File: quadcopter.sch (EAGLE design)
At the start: 11 parts, among them J1 AVR_SPI_PRG_6NS, U1 ATMEGA128RFA1

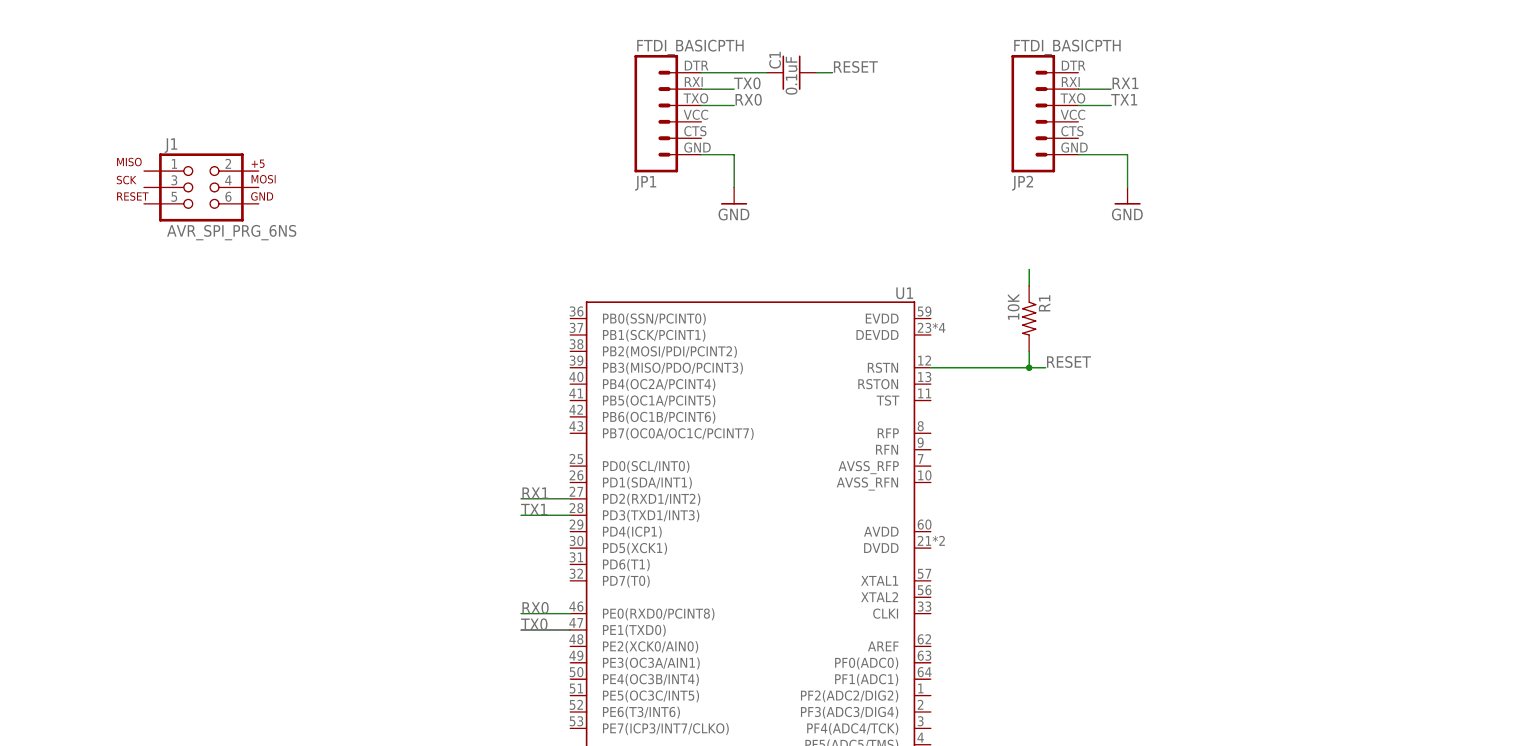
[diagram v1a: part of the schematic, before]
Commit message: finished, for the most part, microcontroller section
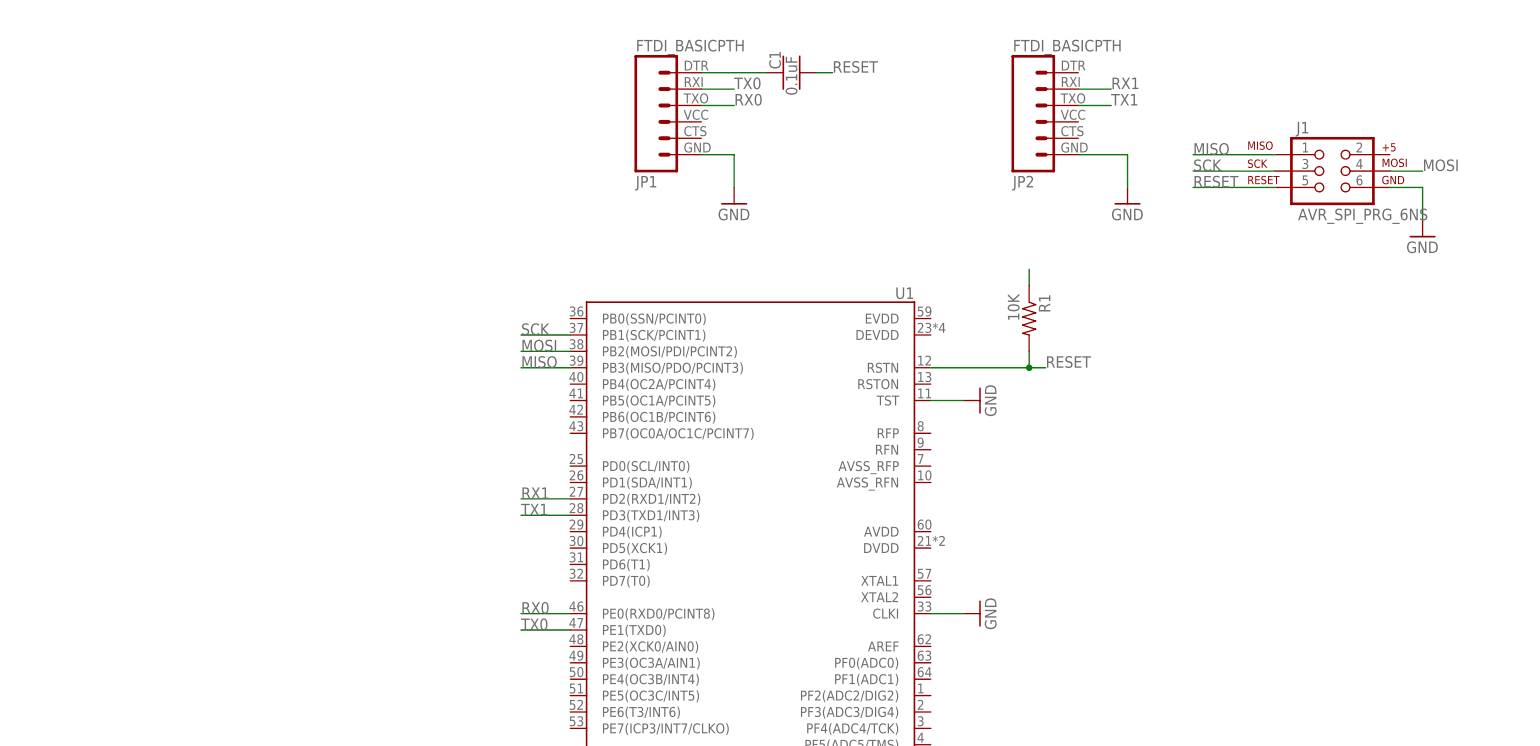
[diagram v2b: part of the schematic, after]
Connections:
- new net MISO: U1.PB3(MISO/PDO/PCINT3)
- new net MOSI: U1.PB2(MOSI/PDI/PCINT2)
- new net N$11: J1.3
- new net N$12: J1.5
- new net N$8: J1.1
- new net N$9: J1.4
- new net SCK: U1.PB1(SCK/PCINT1)
- net GND: now also J1.6, U1.CLKI, U1.TST
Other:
- moved on the sheet: J1
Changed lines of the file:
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@@
 <part name="R1" library="quadparts_prebuilt" deviceset="RESISTOR_" device="SMD-2012-0805-10K" value="10K"/>
 <part name="GND2" library="quadparts_prebuilt" deviceset="GND" device=""/>
+<part name="GND3" library="quadparts_prebuilt" deviceset="GND" device=""/>
+<part name="GND4" library="quadparts_prebuilt" deviceset="GND" device=""/>
+<part name="GND5" library="quadparts_prebuilt" deviceset="GND" device=""/>
 </parts>
 <sheets>
@@
 <instance part="JP1" gate="G$1" x="-71.12" y="12.7" rot="MR180"/>
 <instance part="JP2" gate="G$1" x="-12.7" y="12.7" rot="MR180"/>
-<instance part="J1" gate="G$1" x="-144.78" y="0"/>
+<instance part="J1" gate="G$1" x="30.48" y="2.54"/>
 <instance part="U$1" gate="G$1" x="-20.32" y="60.96"/>
 <instance part="GND1" gate="1" x="-60.96" y="-2.54"/>
@@
 <instance part="R1" gate="G$1" x="-15.24" y="-20.32" rot="R270"/>
 <instance part="GND2" gate="1" x="0" y="-2.54"/>
+<instance part="GND3" gate="1" x="45.72" y="-7.62"/>
+<instance part="GND4" gate="1" x="-22.86" y="-33.02" rot="R90"/>
+<instance part="GND5" gate="1" x="-22.86" y="-66.04" rot="R90"/>
 </instances>
 <busses>
@@
 <wire x1="-7.62" y1="5.08" x2="0" y2="5.08" width="0.1524" layer="91"/>
 <wire x1="0" y1="5.08" x2="0" y2="0" width="0.1524" layer="91"/>
+</segment>
+<segment>
+<pinref part="J1" gate="G$1" pin="6"/>
+<pinref part="GND3" gate="1" pin="GND"/>
+<wire x1="40.64" y1="0" x2="45.72" y2="0" width="0.1524" layer="91"/>
+<wire x1="45.72" y1="0" x2="45.72" y2="-5.08" width="0.1524" layer="91"/>
+</segment>
+<segment>
+<pinref part="U1" gate="G$1" pin="TST"/>
+<pinref part="GND4" gate="1" pin="GND"/>
+<wire x1="-30.48" y1="-33.02" x2="-25.4" y2="-33.02" width="0.1524" layer="91"/>
+</segment>
+<segment>
+<pinref part="U1" gate="G$1" pin="CLKI"/>
+<pinref part="GND5" gate="1" pin="GND"/>
+<wire x1="-30.48" y1="-66.04" x2="-25.4" y2="-66.04" width="0.1524" layer="91"/>
 </segment>
 </net>
@@
 <pinref part="R1" gate="G$1" pin="2"/>
 <wire x1="-15.24" y1="-25.4" x2="-15.24" y2="-27.94" width="0.1524" layer="91"/>
+<label x="10.16" y="0" size="1.778" layer="95"/>
 </segment>
 </net>
@@
 </segment>
 </net>
+<net name="MOSI" class="0">
+<segment>
+<pinref part="U1" gate="G$1" pin="PB2(MOSI/PDI/PCINT2)"/>
+<wire x1="-86.36" y1="-25.4" x2="-93.98" y2="-25.4" width="0.1524" layer="91"/>
+<label x="45.72" y="2.54" size="1.778" layer="95"/>
+<label x="-93.98" y="-25.4" size="1.778" layer="95"/>
+</segment>
+</net>
+<net name="N$9" class="0">
+<segment>
+<pinref part="J1" gate="G$1" pin="4"/>
+<wire x1="40.64" y1="2.54" x2="45.72" y2="2.54" width="0.1524" layer="91"/>
+</segment>
+</net>
+<net name="N$8" class="0">
+<segment>
+<pinref part="J1" gate="G$1" pin="1"/>
+<wire x1="22.86" y1="5.08" x2="10.16" y2="5.08" width="0.1524" layer="91"/>
+</segment>
+</net>
+<net name="MISO" class="0">
+<segment>
+<pinref part="U1" gate="G$1" pin="PB3(MISO/PDO/PCINT3)"/>
+<wire x1="-86.36" y1="-27.94" x2="-93.98" y2="-27.94" width="0.1524" layer="91"/>
+<label x="10.16" y="5.08" size="1.778" layer="95"/>
+<label x="-93.98" y="-27.94" size="1.778" layer="95"/>
+</segment>
+</net>
+<net name="SCK" class="0">
+<segment>
+<pinref part="U1" gate="G$1" pin="PB1(SCK/PCINT1)"/>
+<wire x1="-86.36" y1="-22.86" x2="-93.98" y2="-22.86" width="0.1524" layer="91"/>
+<label x="10.16" y="2.54" size="1.778" layer="95"/>
+<label x="-93.98" y="-22.86" size="1.778" layer="95"/>
+</segment>
+</net>
+<net name="N$11" class="0">
+<segment>
+<pinref part="J1" gate="G$1" pin="3"/>
+<wire x1="22.86" y1="2.54" x2="10.16" y2="2.54" width="0.1524" layer="91"/>
+</segment>
+</net>
+<net name="N$12" class="0">
+<segment>
+<pinref part="J1" gate="G$1" pin="5"/>
+<wire x1="22.86" y1="0" x2="10.16" y2="0" width="0.1524" layer="91"/>
+</segment>
+</net>

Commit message: Sort of finished motor driver sch
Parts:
- added BATT1: BATTERY-HUBSAN-W/HOLDER, quadparts_prebuilt:BATTERY-HUBSAN-W/HOLDER
- added C2, C4, C6, C8: 100uF, quadparts_prebuilt:CAPACITOR-POL_SMD-7043-D_TANTALUM-220UF
- added C3, C5, C7, C9: 1uF, quadparts_prebuilt:CAPACITOR-NP_SMD-2012-0805_CERAMIC-1UF
- added D1, D2, D3, D4: 20V-500MA, quadparts_prebuilt:DIODE-SCHOTTKY_SMD-SOD123
- added J2: (no value), quadparts_connie:MALE_HEADER_2POS-2X1-0.1IN
- added Q1, Q2, Q3, Q4: (no value), quadparts_connie:N_MOSFET_SI2302CDS_T1_E3
- added R2, R4, R6, R8: 100R, quadparts_prebuilt:RESISTOR_SMD-2012-0805-100
- added R3, R5, R7, R9: 10K 1/10W, quadparts_prebuilt:RESISTOR_SMD-2012-0805-100
- added U$6: MOTOR_PADS, quadparts_prebuilt:MOTOR_PADS
- U$3: value MOTOR_PADS -> TPS73633-DBVT; device quadparts_prebuilt:MOTOR_PADS -> quadparts_prebuilt:TPS73633-DBVT
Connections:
- new net FILTERED: Q1.G, Q2.G, Q3.G, Q4.G, R2.2, R3.2, R4.2, R5.2, R6.2, R7.2, R8.2, R9.2
- new net FLYBACK: D1.A, D2.A, D3.A, D4.A, Q1.D, Q2.D, Q3.D, Q4.D, U$2.V-, U$4.V-, U$5.V-, U$6.V-
- new net N$10: C2.+, D1.C, U$2.V+
- new net N$13: C4.+, D2.C, U$4.V+
- new net N$14: C6.+, D3.C, U$5.V+
- new net N$15: C8.+, D4.C, U$6.V+
- new net N$16: U1.PB5(OC1A/PCINT5)
- new net PB5: C3.1, C5.1, C7.1, C9.1, R2.1, R4.1, R6.1, R8.1
- new net PE3: U1.PE3(OC3A/AIN1)
- new net PE4: U1.PE4(OC3B/INT4)
- new net PE5: U1.PE5(OC3C/INT5)
- net GND: now also C2.-, C3.2, C4.-, C5.2, C6.-, C7.2, C8.-, C9.2, Q1.S, Q2.S, Q3.S, Q4.S, R3.1, R5.1, R7.1, R9.1
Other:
- note added: "Filter"
- note added: "Flyback"
- moved on the sheet: R1, U$2, U$4, U$5, U1

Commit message: added stuff
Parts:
- added B1: BALUN0805, quadparts_prebuilt:BALUN0805
- added C10, C11, C12, C13: 1uF, quadparts_prebuilt:CAPACITOR-NP_SMD-2012-0805_CERAMIC-1UF
- added C14, C15: 12pF, quadparts_prebuilt:CAPACITOR-NP_SMD-2012-0805_CERAMIC-1UF
- added C16, C17: JUMP, quadparts_prebuilt:CAPACITOR-NP_SMD-2012-0805_CERAMIC
- added C18: 22pF, quadparts_prebuilt:CAPACITOR-NP_SMD-2012-0805_CERAMIC-22PF
- added C19: 0.75pF, quadparts_prebuilt:CAPACITOR-NP_SMD-2012-0805_CERAMIC-0.75PF
- added U$7: NET_BRIDGE, quadparts_jason:NET_BRIDGE
- added Y1: 16MHz, quadparts_prebuilt:CRYSTAL5X3
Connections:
- removed net N$15: C8.+, D4.C, U$6.V+
- new net 3V: C11.1, R1.1, U$3.OUT, U1.DEVDD, U1.EVDD
- new net BAT_GND: BATT1.N, C2.-, C3.2, C4.-, C5.2, C6.-, C7.2, C8.-, C9.2, Q1.S, Q2.S, Q3.S, Q4.S, R3.1, R5.1, R7.1, R9.1, U$7.P$2
- new net EN: J2.1, U$3.EN
- new net N$21: C16.1, U1.RFP
- new net N$22: C17.1, U1.RFN
- new net N$23: B1.IN, C16.2
- new net N$24: B1.GND@5, C17.2
- new net N$25: C18.1
- new net RFANT: B1.OUT1, C19.2, U$1.SIGNAL
- new net VBAT: BATT1.P, C10.1, C2.+, C4.+, C6.+, C8.+, D1.C, D2.C, D3.C, D4.C, U$2.V+, U$3.IN, U$4.V+, U$5.V+, U$6.V+
- net GND: now also B1.OUT2, C10.2, C11.2, C12.2, C13.2, C14.2, C15.2, C18.2, C19.1, J2.2, U$3.GND, U$3.NC/FB, U$7.P$1, U1.AVSS, U1.AVSS_RFN, U1.AVSS_RFP, U1.DVSS, U1.PG3(TOSC2), U1.PG4(TOSC1); no longer C2.-, C3.2, C4.-, C5.2, C6.-, C7.2, C8.-, C9.2, Q1.S, Q2.S, Q3.S, Q4.S, R3.1, R5.1, R7.1, R9.1
- net N$10: now also C12.1, U1.AVDD; no longer C2.+, D1.C, U$2.V+
- net N$13: now also C13.1, U1.DVDD; no longer C4.+, D2.C, U$4.V+
- net N$14: now also C14.1, U1.XTAL2, Y1.1; no longer C6.+, D3.C, U$5.V+
- net N$5: now also C15.1, U1.XTAL1, Y1.2; no longer R1.1
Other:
- moved on the sheet: BATT1, C2, C3, C4, C5, C6, C7, C8, C9, D1, D2, D3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

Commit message: added more stuff
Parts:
- removed U$7: NET_BRIDGE, quadparts_jason:NET_BRIDGE
- added C20, C21, C22, C23: 100nF, quadparts_prebuilt:CAPACITOR-NP_SMD-2012-0805_CERAMIC
- added C24: 10nF(16V), quadparts_prebuilt:CAPACITOR-NP_SMD-2012-0805_CERAMIC
- added J3: (no value), quadparts_prebuilt:SIP-10_TH-254X10
- added NET_BRIDGE: NET_BRIDGE, quadparts_jason:NET_BRIDGE
- added U2: IMU_LSM9DS1TR, quadparts_connie:IMU_LSM9DS1TR
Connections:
- new net N$15: C21.1, U2.C1
- new net N$17: C24.1, U2.CAP
- new net N$18: U2.CS_A/G
- new net SCL: J3.1
- new net SDA: J3.2
- net 3V: now also C20.1, C22.1, C23.1, J3.7, U2.CS_M, U2.VDD@1, U2.VDD@2, U2.VDDIO@1, U2.VDDIO@2
- net BAT_GND: now also J3.9, NET_BRIDGE.P$2; no longer U$7.P$2
- net GND: now also C20.2, C21.2, C22.2, C23.2, C24.2, J3.10, NET_BRIDGE.P$1, U2.GND@1, U2.GND@2, U2.RES@1, U2.RES@2, U2.RES@3, U2.RES@4, U2.RES@5; no longer U$7.P$1
- net PB5: now also J3.6
- net PE3: now also J3.4
- net PE4: now also J3.3
- net PE5: now also J3.5
- net VBAT: now also J3.8
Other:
- moved on the sheet: B1, BATT1, C1, C10, C11, C12, C13, C14, C15, C16, C17, C18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

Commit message: tiny changes
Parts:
- added D5: Yellow, LEDs:LED_VLMX51Z1AAYELLOW
- added D6: Red, LEDs:LED_VLMX51Z1AARED
- added D7: Blue, LEDs:LED_OVS5MXBCR4BLUE
- added D8: Green, LEDs:LED_OVS5MXBCR4GREEN
- added R10, R11: (no value), quadparts_prebuilt:RESISTOR_SMD-2012-0805
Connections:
- new net N$19: D5.C, D6.A
- new net N$20: D7.A, U1.PG0(DIG3)
- new net N$26: D8.A, U1.PG1(DIG1)
- net 3V: now also R10.2, R11.2
- net BAT_GND: now also D6.C
- net GND: now also D7.C, D8.C
- net SCL: now also R10.1, U1.PD0(SCL/INT0), U2.SCL/SPC
- net SDA: now also R11.1, U1.PD1(SDA/INT1), U2.SDA/SDI/SDO
- net VBAT: now also D5.A
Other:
- moved on the sheet: C6, C7, D3, J3, Q3, R6, R7, U$5

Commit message: added current-limiting resistors
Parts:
- removed D7: Blue, LEDs:LED_OVS5MXBCR4BLUE
- removed D8: Green, LEDs:LED_OVS5MXBCR4GREEN
- added D10: Green, LEDs:LED_OVS5MXBCR4GREEN
- added D9: Blue, LEDs:LED_OVS5MXBCR4BLUE
- added R12, R13, R14: 5, quadparts_prebuilt:RESISTOR_SMD-2012-0805
- D5: value Yellow -> Red; device LEDs:LED_VLMX51Z1AAYELLOW -> LEDs:LED_VLMX51Z1AARED
- D6: value Red -> Yellow; device LEDs:LED_VLMX51Z1AARED -> LEDs:LED_VLMX51Z1AAYELLOW
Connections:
- removed net N$18: U2.CS_A/G
- new net N$27: D10.A, D9.A, R12.2
- new net N$28: D6.A, R14.2
- net 3V: now also U2.CS_A/G
- net BAT_GND: now also D10.C, D9.C; no longer D6.C
- net GND: now also D5.C, D6.C; no longer D7.C, D8.C
- net N$19: now also D5.A, R13.1; no longer D5.C, D6.A
- net N$20: now also R14.1; no longer D7.A
- net N$26: now also R13.2; no longer D8.A
- net VBAT: now also R12.1; no longer D5.A
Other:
- moved on the sheet: D5, D6
